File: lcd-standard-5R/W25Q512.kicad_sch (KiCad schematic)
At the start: 3 parts, among them U1 MT25Q

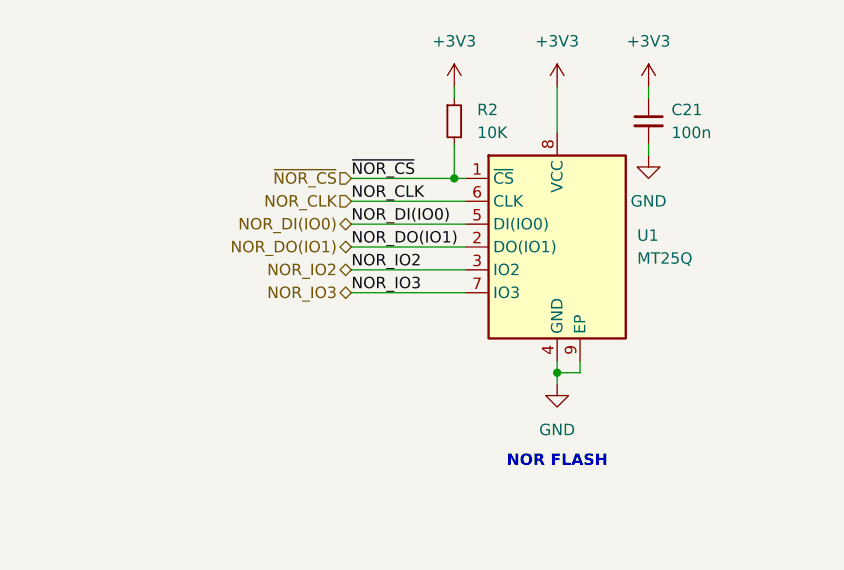
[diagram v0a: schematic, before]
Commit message: Add QSPI Flash trace length matching to 5 inch LCD
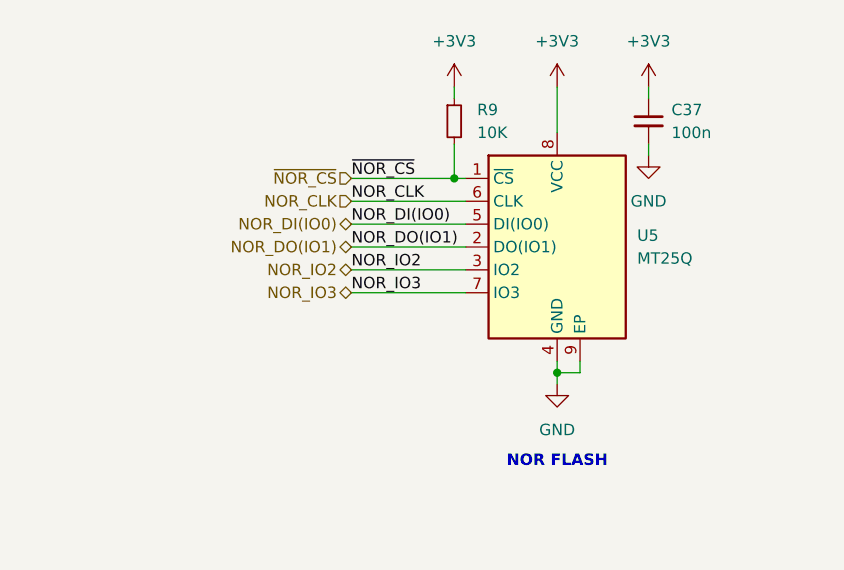
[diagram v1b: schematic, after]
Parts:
- renumbered C21 to C37, R2 to R9, U1 to U5
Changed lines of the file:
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@@
 (kicad_sch
-	(version 20231120)
+	(version 20250114)
 	(generator "eeschema")
-	(generator_version "8.0")
+	(generator_version "9.0")
 	(paper "A4")
+	(text "NOR FLASH"
+		(exclude_from_sim no)
+		(at 140.97 119.126 0)
+		(effects
+			(font
+				(size 1.27 1.27)
+				(thickness 0.254)
+				(bold yes)
+			)
+		)
+	)
 	(junction
 		(at 140.97 109.22)
@@
 		)
 	)
-	(text "NOR FLASH"
-		(exclude_from_sim no)
-		(at 140.97 119.126 0)
-		(effects
-			(font
-				(size 1.27 1.27)
-				(thickness 0.254)
-				(bold yes)
-			)
-		)
-	)
 	(label "NOR_CLK"
 		(at 118.11 90.17 0)
-		(fields_autoplaced yes)
 		(effects
 			(font
@@
 	(label "NOR_DI(IO0)"
 		(at 118.11 92.71 0)
-		(fields_autoplaced yes)
 		(effects
 			(font
@@
 	(label "NOR_DO(IO1)"
 		(at 118.11 95.25 0)
-		(fields_autoplaced yes)
 		(effects
 			(font
@@
 	(label "~{NOR_CS}"
 		(at 118.11 87.63 0)
-		(fields_autoplaced yes)
 		(effects
 			(font
@@
 	(label "NOR_IO3"
 		(at 118.11 100.33 0)
-		(fields_autoplaced yes)
 		(effects
 			(font
@@
 	(label "NOR_IO2"
 		(at 118.11 97.79 0)
-		(fields_autoplaced yes)
 		(effects
 			(font
@@
 		(shape bidirectional)
 		(at 118.11 97.79 180)
-		(fields_autoplaced yes)
 		(effects
 			(font
@@
 		(shape bidirectional)
 		(at 118.11 92.71 180)
-		(fields_autoplaced yes)
 		(effects
 			(font
@@
 		(shape bidirectional)
 		(at 118.11 100.33 180)
-		(fields_autoplaced yes)
 		(effects
 			(font
@@
 		(shape input)
 		(at 118.11 90.17 180)
-		(fields_autoplaced yes)
 		(effects
 			(font
@@
 		(shape bidirectional)
 		(at 118.11 95.25 180)
-		(fields_autoplaced yes)
 		(effects
 			(font
@@
 		(shape input)
 		(at 118.11 87.63 180)
-		(fields_autoplaced yes)
 		(effects
 			(font
@@
 		(dnp no)
 		(fields_autoplaced yes)
-		(property "Reference" "#PWR017"
+		(property "Reference" "#PWR060"
 			(at 151.13 91.44 0)
 			(effects
@@
 		(dnp no)
 		(fields_autoplaced yes)
-		(property "Reference" "#PWR038"
+		(property "Reference" "#PWR058"
 			(at 140.97 116.84 0)
 			(effects
@@
 		(dnp no)
 		(fields_autoplaced yes)
-		(property "Reference" "C21"
+		(property "Reference" "C37"
 			(at 153.67 80.0163 0)
 			(effects
@@
 		(dnp no)
 		(fields_autoplaced yes)
-		(property "Reference" "#PWR016"
+		(property "Reference" "#PWR059"
 			(at 151.13 81.28 0)
 			(effects
@@
 		(dnp no)
 		(fields_autoplaced yes)
-		(property "Reference" "R2"
+		(property "Reference" "R9"
 			(at 132.08 80.0099 0)
 			(effects
@@
 		(dnp no)
 		(fields_autoplaced yes)
-		(property "Reference" "#PWR09"
+		(property "Reference" "#PWR056"
 			(at 129.54 81.28 0)
 			(effects
@@
 		(dnp no)
 		(fields_autoplaced yes)
-		(property "Reference" "#PWR037"
+		(property "Reference" "#PWR057"
 			(at 140.97 81.28 0)
 			(effects
@@
 		(dnp no)
 		(fields_autoplaced yes)
-		(property "Reference" "U1"
+		(property "Reference" "U5"
 			(at 149.86 93.9799 0)
 			(effects

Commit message: Replace QSPI Flash footprint
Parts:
- U5: footprint Package_SON:WSON-8-1EP_8x6mm_P1.27mm_EP3.4x4.3mm -> W25Q256JVEIQ:SON127P800X600X80-9N
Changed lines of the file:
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@@
 			)
 		)
-		(property "Footprint" "Package_SON:WSON-8-1EP_8x6mm_P1.27mm_EP3.4x4.3mm"
+		(property "Footprint" "W25Q256JVEIQ:SON127P800X600X80-9N"
 			(at 140.97 95.25 0)
 			(effects

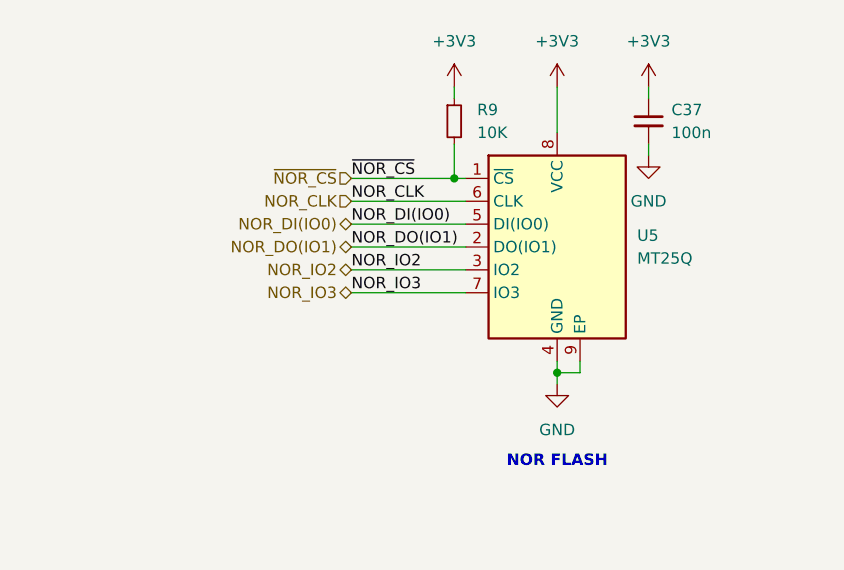
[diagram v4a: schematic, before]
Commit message: LCD-5inch, SDRAM,QSPI,SDRCARD,EEPROM finished, 90% left
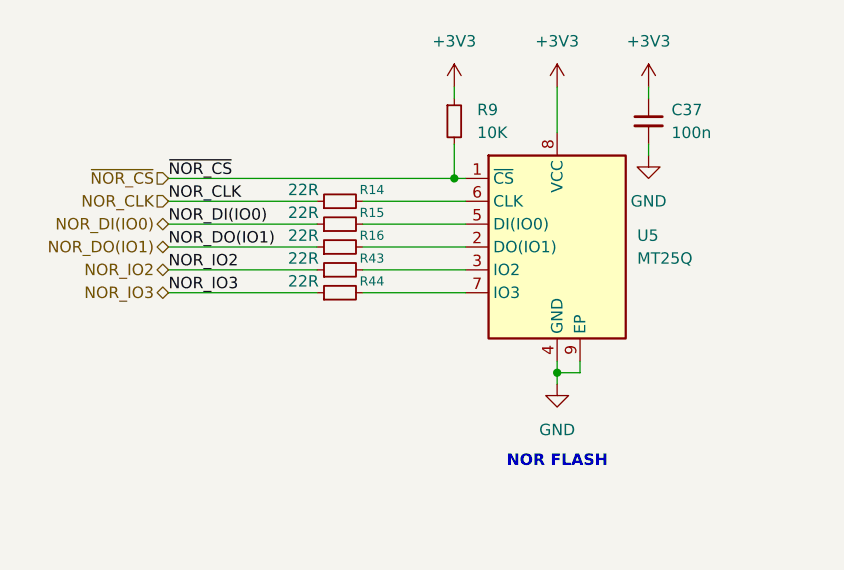
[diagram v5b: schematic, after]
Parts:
- added R14, R15, R16, R43, R44: 22R, Resistor_SMD:R_0201_0603Metric, symbol Device:R_Small
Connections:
- net NOR_CLK: now also R14.1; no longer U5.6 (CLK)
- net NOR_DI(IO0): now also R15.1; no longer U5.5 (DI(IO0))
- net NOR_DO(IO1): now also R16.1; no longer U5.2 (DO(IO1))
- net NOR_IO2: now also R43.1; no longer U5.3 (IO2)
- net NOR_IO3: now also R44.1; no longer U5.7 (IO3)
- new net: R15.2, U5.5 (DI(IO0))
- new net: R14.2, U5.6 (CLK)
- new net: R43.2, U5.3 (IO2)
- new net: R44.2, U5.7 (IO3)
- new net: R16.2, U5.2 (DO(IO1))

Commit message: Need checkout the gerber before sending to JLCPCB
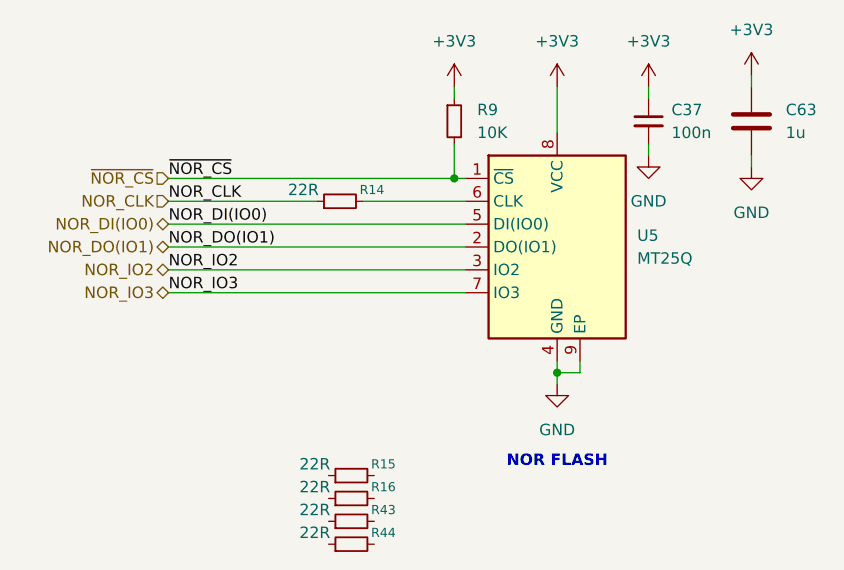
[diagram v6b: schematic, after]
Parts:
- added C63: 1u, Capacitor_SMD:C_0603_1608Metric, symbol Device:C
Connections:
- net +3V3: now also C63.1
- net GND: now also C63.2
- net NOR_DI(IO0): now also U5.5 (DI(IO0)); no longer R15.1
- net NOR_DO(IO1): now also U5.2 (DO(IO1)); no longer R16.1
- net NOR_IO2: now also U5.3 (IO2); no longer R43.1
- net NOR_IO3: now also U5.7 (IO3); no longer R44.1
- net at R15.2: no longer U5.5 (DI(IO0))
- net at R43.2: no longer U5.3 (IO2)
- net at R44.2: no longer U5.7 (IO3)
- net at R16.2: no longer U5.2 (DO(IO1))
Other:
- moved on the sheet: R15, R16, R43, R44
